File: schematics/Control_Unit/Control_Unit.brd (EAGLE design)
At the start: 49.8 x 49.8 mm, 239 parts, among them IC1 74HCT32N, IC10 74HC74N, IC100 74HCT374N, IC101 74HCT08N, IC102 74HC151N, IC103 74HC373N, IC105 74HC151N, IC106 74HC151N, IC108 74HCT32N, IC11 74HC74N, IC110 74HCT32N, IC111 74HC151N, IC112 74HCT32N, IC113 74HC151N, IC114 74HC151N, IC115 74HC151N, IC116 74HC373N, IC117 74HC74N, IC12 74AC08N, IC124 74HCT32N, IC125 74HCT08N, IC126 74AC157N, IC127 74HCT08N, IC128 74AC08N, IC129 74AC08N, IC13 74AC08N, IC134 74HCT08N, IC135 74HCT08N, IC136 74HCT08N, IC14 74HC74N, IC141 74HCT32N, IC15 74HC74N, IC16 74AC08N, IC168 74HCT32N, IC169 74HCT32N, IC17 74HCT32N, IC172 74HCT32N, IC173 74HCT32N, IC175 74HC193N, IC176 74HC193N, IC177 74HC193N, IC178 74HC193N, IC179 74HC193N, IC18 74AC08N, IC180 74HC193N, IC181 74HC193N, IC182 74HC193N, IC19 74AC08N, IC190 74HCT32N, IC191 74HCT32N, IC2 74HCT32N, IC20 74AC08N, IC21 74AC08N, IC22 74HCT32N, IC23 74HCT08N, IC24 74HCT08N, IC26 74HCT08N, IC27 74HCT08N, IC28 74HCT08N, IC29 74HCT32N, IC3 74HC151N, IC30 74HCT08N, IC31 74HCT00N, IC32 74HCT32N, IC33 74HCT32N, IC34 74HCT08N, IC35 74HCT04N, IC36 74HCT32N, IC38 74HCT08N, IC39 74HCT08N, IC4 74AC08N, IC40 74HCT08N, IC41 74HCT08N, IC42 74HC373N, IC43 74HCT04N, IC44 74ACT157N, IC46 74ACT157N, IC47 74HCT04N, IC48 74ACT02N, IC49 74AC86N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

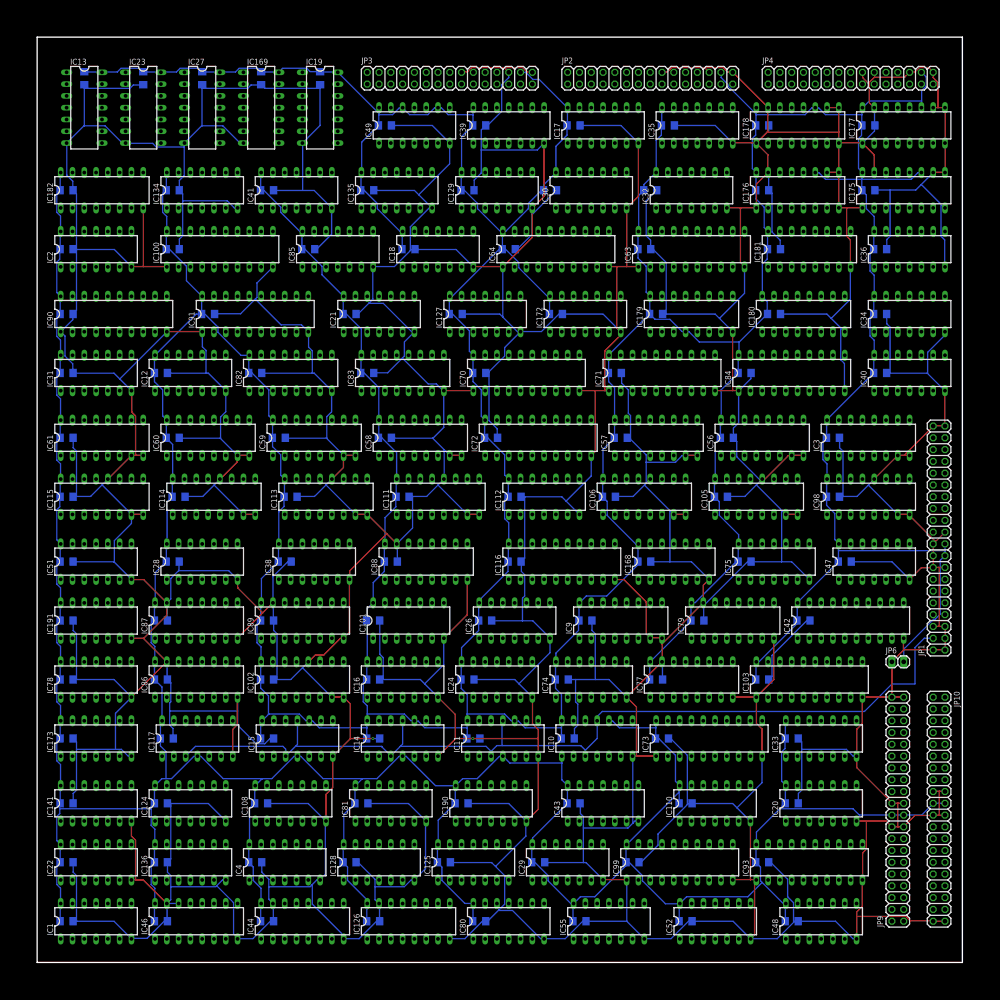
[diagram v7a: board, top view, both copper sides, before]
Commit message: fix. gonna try to reduce cycles to 8 per instruction now
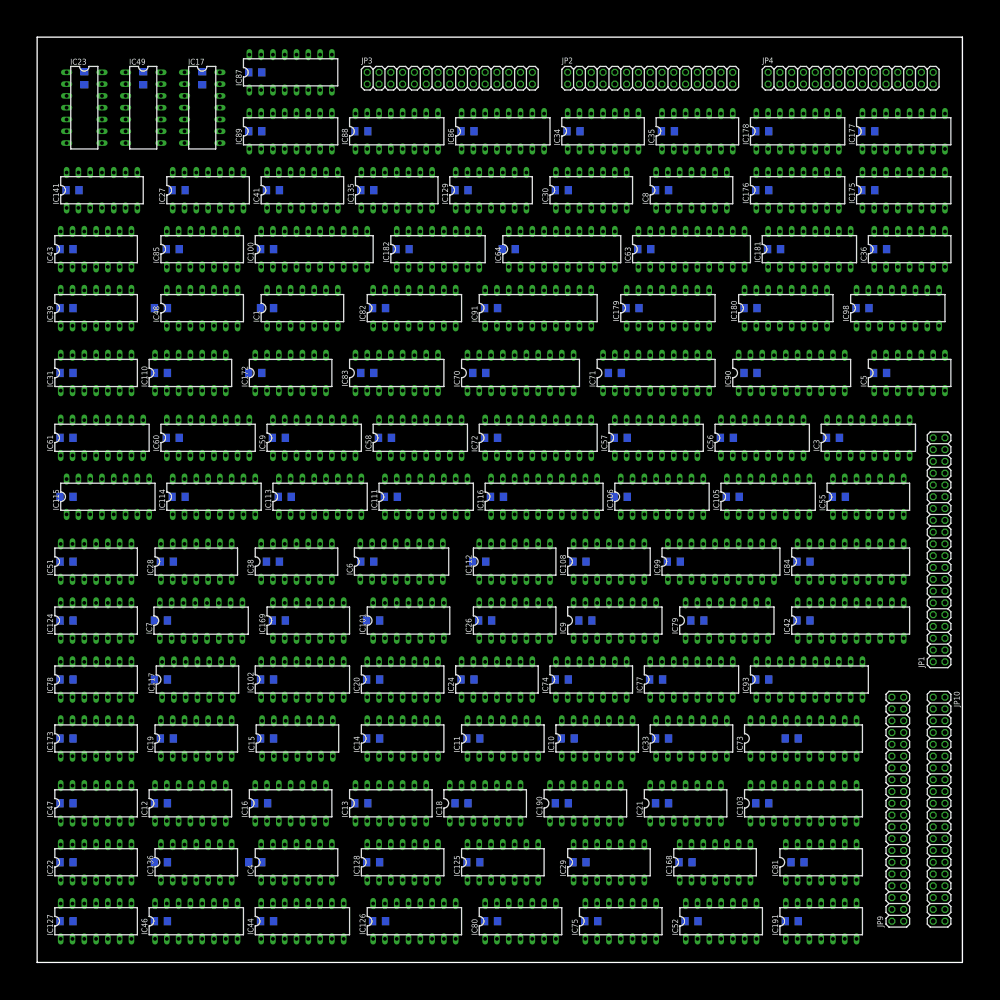
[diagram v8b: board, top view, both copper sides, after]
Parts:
- removed IC134: 74HCT08N, 74xx-eu:DIL14
- removed IC2: 74HCT32N, 74xx-eu:DIL14
- removed JP6: (no value), pinhead:1X02
- added IC6, IC7: 74HC193N, custom_parts:DIL16
- IC5: value 74HCT08N -> 74ACT02N
- IC8: value 74HCT32N -> 74ACT02N
- moved IC48 46.9 mm to (8.89, 35.2)
- moved IC47 43.9 mm to (3.17, 8.57)
- moved IC191 42.3 mm to (42.2, 2.22)
- moved IC13 40.9 mm to (19.1, 8.57), turned to 0 degrees
- moved IC43 40.5 mm to (3.17, 38.4)
- moved IC127 38.8 mm to (3.17, 2.22)
- moved IC90 36.7 mm to (40.6, 31.8)
- moved IC110 36.5 mm to (8.26, 31.8)
- moved IC1 34.8 mm to (14.3, 35.2)
- moved IC19 34.6 mm to (8.57, 12.1), turned to 0 degrees
- moved IC86 33.8 mm to (25.1, 44.8)
- moved IC141 33.0 mm to (3.49, 41.6)
- moved IC21 31.1 mm to (34.9, 8.57)
- moved IC87 30.0 mm to (13.7, 47.9)
- moved IC18 30.0 mm to (24.1, 8.57)
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- renumbered IC32 to IC8, IC40 to IC5
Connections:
- net ALU_NR3_ENABLE renamed ALU_NR3_ENABLE_ALU
- net ALU_NR4_ENABLE renamed ALU_NR4_ENABLE_ALU
- removed net INPUT_REG_IS_OUTPUT_REG: IC43.10, IC5.9
- removed net N$128: IC101.4, IC49.8
- removed net N$144: IC181.4, IC75.8
- removed net N$145: IC180.13, IC75.10
- removed net N$164: IC127.9, IC47.10
- removed net N$206: IC108.3, IC80.1
- removed net N$222: IC129.2, IC129.5, IC43.6
- removed net N$242: IC179.13, IC180.4
- removed net N$44: IC31.4, IC35.10
- removed net NOT_USED2: IC134.3
- removed net NOT_USED3: IC134.6
- removed net NOT_USED4: IC134.8
- removed net NOT_USED5: IC134.11
- new net !IR_DATA_OUT_7: IC101.12, IC127.9, IC36.12, IC47.10
- new net !OPCODE_5: IC129.2, IC129.5, IC43.6, IC75.10
- new net N$77: IC6.12, IC7.5
- new net N$80: IC112.3, IC80.9
- new net TIMER_CLOCK: IC6.5, JP1.3
- new net TIMER_REG_0: IC115.12, IC6.3
- new net TIMER_REG_1: IC114.12, IC6.2
- new net TIMER_REG_2: IC113.12, IC6.6
- new net TIMER_REG_3: IC111.12, IC6.7
- new net TIMER_REG_4: IC106.12, IC7.3
- new net TIMER_REG_5: IC105.12, IC7.2
- new net TIMER_REG_6: IC7.6, IC98.12
- new net TIMER_REG_7: IC102.12, IC7.7
- new net UNUSED: IC34.6
- net !REGISTER_RESET: now also IC6.14, IC7.14
- net ALU_CARRY_BIT: now also IC34.12, JP1.16; no longer IC5.1, JP1.7
- net ALU_CARRY_IN: now also IC34.11; no longer IC5.3
- net ALU_CARRY_OUT: now also IC101.9; no longer IC101.12
- net DATA0: now also IC77.2; no longer IC77.3
- net DATA1: now also IC77.5; no longer IC77.6
- net DATA2: now also IC77.11; no longer IC77.10
- net DATA3: now also IC77.14; no longer IC77.13
- net DATA4: now also IC79.2; no longer IC79.3
- net DATA5: now also IC79.5; no longer IC79.6
- net DATA6: now also IC79.11; no longer IC79.10
- net DATA7: now also IC79.14; no longer IC79.13
- net DATA_BUS_ENABLE_LATCH: now also IC34.3; no longer IC101.3
- net FILL_LR_H_SAVE_LR: now also IC5.11; no longer IC2.12
- net FILL_LR_L_SAVE_LR: now also IC5.8; no longer IC1.4
- net FILL_PC_H_RET: now also IC1.4; no longer IC1.1
- net FILL_PC_L_JMP_O: now also IC101.10; no longer IC101.13
- net FILL_PTR_H_SET_PTR: now also IC5.3; no longer IC2.5
- net FILL_PTR_L_SET_PTR: now also IC169.10; no longer IC2.2
- net GND: now also IC6.1, IC6.10, IC6.15, IC6.8, IC6.9, IC7.1, IC7.10, IC7.15, IC7.8, IC7.9, JP1.11, JP1.13, JP1.7, JP1.9; no longer IC102.12, IC105.12, IC106.12, IC111.12, IC113.12, IC114.12, IC115.12, IC134.7, IC2.7, IC98.12, JP1.16, JP1.18, JP1.20, JP1.3, JP6.1
- net INPUT_REG0/OPCODE_5/OPCODE_4_IS_NULL: now also IC101.1, IC31.5; no longer IC34.1, IC5.5
- net INPUT_REG2: now also IC34.4; no longer IC134.1, IC134.4
- net INPUT_REG3: no longer IC134.12, IC134.9
- net INPUT_REG_IS_NOT_OUTPUT_REG: now also IC5.5; no longer IC43.11
- net IR_DATA_OUT_7: now also IC101.4; no longer IC101.9, IC36.12, IC49.10
- net LR_H_LOAD_INPUT_NOT: now also IC5.13; no longer IC2.11
- net LR_H_LOAD_INPUT_TABLE_1: now also IC5.12; no longer IC2.13
- net LR_L_LOAD_INPUT_NOT: now also IC5.10; no longer IC1.6
- net LR_L_LOAD_INPUT_TABLE_1: now also IC5.9; no longer IC1.5
- net N$11: now also IC169.8, IC43.11; no longer IC110.6, IC52.13
- net N$12: now also IC34.8, IC35.11; no longer IC49.13, IC5.11
- net N$121: now also IC52.12; no longer IC169.9
- net N$13: now also IC26.12, IC80.8; no longer IC108.1, IC112.3
- net N$139: now also IC101.13, IC101.8; no longer IC101.10, IC101.11
- net N$141: now also IC49.8; no longer IC26.11
- net N$142: now also IC49.9; no longer IC26.12
- net N$185: now also IC55.5; no longer IC108.13
- net N$187: now also IC55.4; no longer IC108.12
- net N$190: now also IC108.11, IC108.2; no longer IC55.6, IC80.10
- net N$192: now also IC108.1; no longer IC80.9
- net N$193: now also IC108.3; no longer IC80.8
- net N$2: now also IC110.4; no longer IC52.12
- net N$20: now also IC55.6; no longer IC108.11
- net N$203: now also IC26.13, IC31.6; no longer IC5.6, IC80.2
- net N$21: now also IC31.4, IC80.10; no longer IC108.2, IC5.4
- net N$219: now also IC75.8; no longer IC31.6
- net N$22: now also IC101.3; no longer IC34.3
- net N$235: no longer IC134.13, IC134.5
- net N$239: now also IC34.5; no longer IC134.10, IC134.2
- net N$252: now also IC52.13; no longer IC169.10
- net N$266: now also IC34.10, IC34.2, IC52.11; no longer IC101.2, IC169.8, IC5.13
- net N$33: now also IC1.6; no longer IC1.3
- net N$45: now also IC26.11, IC5.6; no longer IC5.10, IC80.3
- net N$52: now also IC35.10; no longer IC49.11
- net N$57: now also IC8.6; no longer IC8.5
- net N$64: now also IC8.9; no longer IC8.10
- net N$7: now also IC34.1; no longer IC101.1
- net N$71: now also IC8.12; no longer IC8.13
- net N$9: now also IC8.3; no longer IC8.2
- net N$90: now also IC110.6; no longer IC52.11
- net OPCODE_5: no longer IC31.5
- net OPC_67_OUPUT0/REG0_JMP: now also IC101.2; no longer IC34.2
- net PC_COUNT_UP: now also IC1.3; no longer IC2.8
- net PC_COUNT_UP_FETCH1: now also IC1.1; no longer IC2.9
- net PC_COUNT_UP_FETCH2/CYCL_5: now also IC1.2; no longer IC2.10
- net PC_DATA_OUT_0: now also IC77.3; no longer IC77.2
- net PC_DATA_OUT_1: now also IC77.6; no longer IC77.5
- net PC_DATA_OUT_2: now also IC77.10; no longer IC77.11
- net PC_DATA_OUT_3: now also IC77.13; no longer IC77.14
- net PC_DATA_OUT_4: now also IC79.3; no longer IC79.2
- net PC_DATA_OUT_5: now also IC79.6; no longer IC79.5
- net PC_DATA_OUT_6: now also IC79.10; no longer IC79.11
- net PC_DATA_OUT_7: now also IC79.13; no longer IC79.14
- net PC_H_COUNT_DOWN_JMP_O: now also IC101.6, IC181.4; no longer IC101.8, IC75.9
- net PC_H_COUNT_UP_JMP_O: now also IC101.11, IC49.10; no longer IC101.6, IC26.13
- net PC_H_LOAD_INPUT_TABLE_1: now also IC1.5; no longer IC1.2
- net PTR_H_LOAD_INPUT_NOT: now also IC5.1; no longer IC2.6
- net PTR_L_LOAD_INPUT_NOT: now also IC43.10; no longer IC2.3
- net REG0_ZERO: now also JP1.20; no longer JP1.11
- net REGISTER_OUTPUT_SEL_3: now also IC34.9; no longer IC5.12
- net REG_0_LOAD_INPUT: now also IC8.1; no longer IC8.3
- net REG_0_OUT_2: now also IC108.12; no longer IC55.4
- net REG_0_OUT_3: now also IC108.13; no longer IC55.5
- net REG_1_LOAD_INPUT: now also IC8.4; no longer IC8.6
- net REG_2_LOAD_INPUT: now also IC8.10; no longer IC8.8
- net REG_3_LOAD_INPUT: now also IC8.13; no longer IC8.11
- net SAVE_LR/RET: now also IC75.9; no longer IC35.11
- net SELECT_CARRY_BIT: now also IC34.13; no longer IC5.2
- net SP_DATA_OVER/UNDERFLOW: now also JP1.18; no longer JP1.9
- net TABLE_1_INPUT_PTR_HIGH: now also IC5.2; no longer IC2.4
- net TABLE_1_INPUT_PTR_L: now also IC169.9; no longer IC2.1
- net TABLE_1_INPUT_REG0: now also IC8.2; no longer IC8.1
- net TABLE_1_INPUT_REG1: now also IC8.5; no longer IC8.4
- net TABLE_1_INPUT_REG2: now also IC8.8; no longer IC8.9
- net TABLE_1_INPUT_REG3: now also IC8.11; no longer IC8.12
- net TWO_BYTE_CMD: now also IC5.4; no longer IC5.8
- net VCC: now also IC180.4, IC6.11, IC6.16, IC6.4, IC7.11, IC7.16, IC7.4; no longer IC134.14, IC2.14, IC49.12, IC49.9, JP6.2
- net WRITE_REGB_TO_DBUS_JMP_O: no longer IC110.4
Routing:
- net GND: track 837.1 -> 0.00 mm, vias 2 -> 0
- net VCC: track 521.1 -> 0.00 mm
- net RING_CNTR_CLOCK: track 51.1 -> 0.00 mm
